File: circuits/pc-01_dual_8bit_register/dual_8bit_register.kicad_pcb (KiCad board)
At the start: 2 copper layers, 99.1 x 99.1 mm, 34 parts, among them J1 Conn_01x10, U1 74HC273, U2 74HC273, U3 74HC244, U4 74HC244, U5 74HC244, U6 74HC244

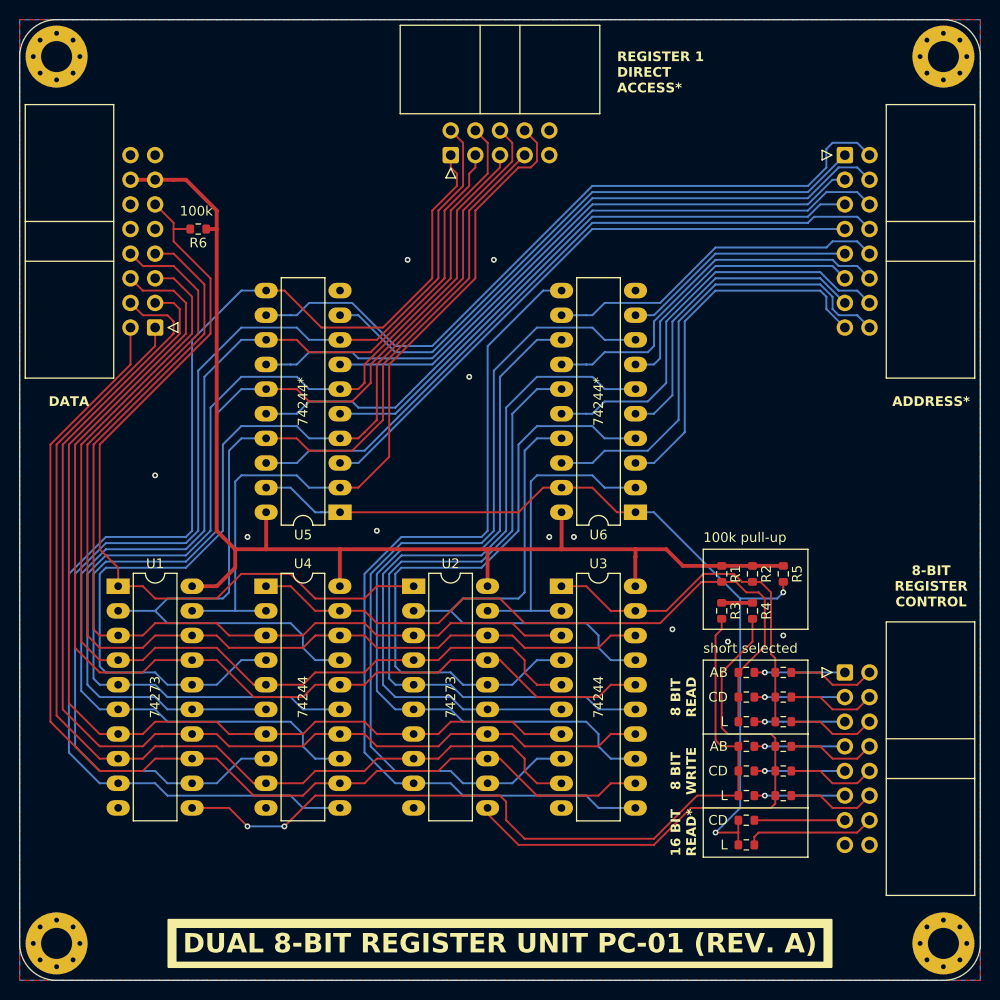
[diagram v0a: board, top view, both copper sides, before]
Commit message: add filter and decoupling capacitors to all boards
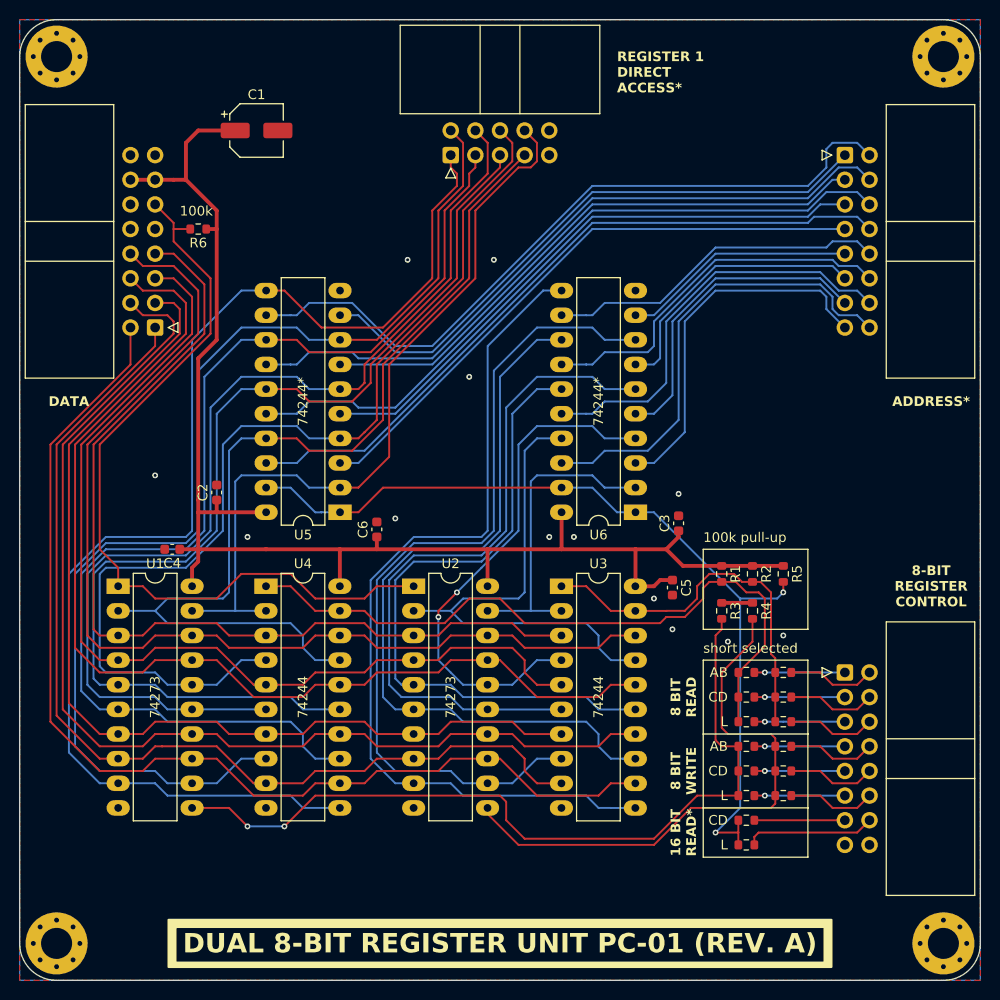
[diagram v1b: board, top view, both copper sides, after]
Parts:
- added C1: C_Polarized, Capacitor_SMD:CP_Elec_5x5.3, F.Cu at (65.1, 34.3)
- added C2: C, Capacitor_SMD:C_0603_1608Metric, F.Cu at (61.0, 71.6)
- added C3: C, Capacitor_SMD:C_0603_1608Metric, F.Cu at (108.6, 74.8)
- added C4: C, Capacitor_SMD:C_0603_1608Metric, F.Cu at (56.4, 77.5)
- added C5: C, Capacitor_SMD:C_0603_1608Metric, F.Cu at (108.0, 81.4)
- added C6: C, Capacitor_SMD:C_0603_1608Metric, F.Cu at (77.5, 75.4)
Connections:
- DATA_BUS1 pad 12: /clock -> unconnected-(DATA_BUS1-Pin_12-Pad12)
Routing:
- net VCC: track 130.4 -> 154.8 mm
- net Net-(U2-Q6): track 65.3 -> 53.8 mm, vias 0 -> 2
- net Net-(U2-Q1): track 70.2 -> 68.6 mm
- net Net-(U2-Q5): track 73.3 -> 71.7 mm
- net Net-(U2-Q4): track 88.1 -> 86.8 mm
- net Net-(U2-Q2): track 80.7 -> 79.4 mm
- net Net-(U2-Q3): track 92.3 -> 91.0 mm
- net Net-(U3-1OE): track 38.6 -> 39.3 mm
- net Net-(U4-1OE): track 71.4 -> 72.1 mm
- net GND: vias 11 -> 13

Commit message: cleanup
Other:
- board text added: "74244 (DRIVER)"
- board text added: "74244* (DRIVER)"
- board text added: "74273 (REGISTER)"
- board text removed: "100k"
- board text removed: "100k pull-up"
- board text removed: "74244"
- board text removed: "74244*"
- board text removed: "74273"
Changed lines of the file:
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@@
 			(disableapertmacros no)
 			(usegerberextensions no)
-			(usegerberattributes yes)
-			(usegerberadvancedattributes yes)
-			(creategerberjobfile yes)
+			(usegerberattributes no)
+			(usegerberadvancedattributes no)
+			(creategerberjobfile no)
 			(dashed_line_dash_ratio 12.000000)
 			(dashed_line_gap_ratio 3.000000)
@@
 			(sketchdnponfab yes)
 			(crossoutdnponfab yes)
-			(subtractmaskfromsilk no)
+			(subtractmaskfromsilk yes)
 			(outputformat 1)
 			(mirror no)
-			(drillshape 1)
+			(drillshape 0)
 			(scaleselection 1)
-			(outputdirectory "")
+			(outputdirectory "./CAM")
 		)
 	)
@@
 	)
 	(gr_line
-		(start 121.92 77.47)
-		(end 121.92 85.725)
-		(stroke
-			(width 0.1)
-			(type default)
-		)
-		(layer "F.SilkS")
-	)
-	(gr_line
 		(start 121.92 96.52)
 		(end 121.92 88.9)
@@
 	)
 	(gr_line
-		(start 111.125 77.47)
-		(end 121.92 77.47)
-		(stroke
-			(width 0.1)
-			(type default)
-		)
-		(layer "F.SilkS")
-	)
-	(gr_line
-		(start 121.92 85.725)
-		(end 111.125 85.725)
-		(stroke
-			(width 0.1)
-			(type default)
-		)
-		(layer "F.SilkS")
-	)
-	(gr_line
 		(start 111.125 96.52)
 		(end 121.92 96.52)
@@
 	)
 	(gr_line
-		(start 111.125 85.725)
-		(end 111.125 77.47)
-		(stroke
-			(width 0.1)
-			(type default)
-		)
-		(layer "F.SilkS")
-	)
-	(gr_line
 		(start 121.92 104.14)
 		(end 121.92 96.52)
@@
 		)
 	)
-	(gr_text "74244"
+	(gr_text "74244 (DRIVER)"
 		(at 100.33 92.71 90)
 		(layer "F.SilkS")
@@
 		)
 	)
-	(gr_text "74244"
+	(gr_text "74244 (DRIVER)"
 		(at 69.85 92.71 90)
 		(layer "F.SilkS")
@@
 		)
 	)
-	(gr_text "100k"
-		(at 57.15 43.18 0)
-		(layer "F.SilkS")
-		(effects
-			(font
-				(size 1 1)
-				(thickness 0.1)
-			)
-			(justify left bottom)
-		)
-	)
 	(gr_text "CD"
 		(at 113.665 92.71 0)
@@
 		)
 	)
-	(gr_text "74273"
+	(gr_text "74273 (REGISTER)"
 		(at 85.09 92.71 90)
 		(layer "F.SilkS")
@@
 		)
 	)
-	(gr_text "74273"
+	(gr_text "74273 (REGISTER)"
 		(at 54.61 92.71 90)
 		(layer "F.SilkS")
@@
 		)
 	)
-	(gr_text "74244*"
+	(gr_text "74244* (DRIVER)"
 		(at 69.85 62.23 90)
 		(layer "F.SilkS")
@@
 		)
 	)
-	(gr_text "100k pull-up"
-		(at 111.125 76.835 0)
-		(layer "F.SilkS")
-		(effects
-			(font
-				(size 1 1)
-				(thickness 0.1)
-			)
-			(justify left bottom)
-		)
-	)
 	(gr_text "short selected"
 		(at 111.125 88.265 0)
@@
 		)
 	)
-	(gr_text "74244*"
+	(gr_text "74244* (DRIVER)"
 		(at 100.33 62.23 90)
 		(layer "F.SilkS")
